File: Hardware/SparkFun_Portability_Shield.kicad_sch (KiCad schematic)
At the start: 39 parts, among them J1 microSD_Friction, SW2 Nav Switch, U4 PCA9557PW, U5 OLED_1.3"

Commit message: Fix nav switch. Adjust silk. Update to v10.
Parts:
- SW2: footprint SparkFun-Switch:Navigation_SMD_9.9x9.9mm -> SparkFun-Switch:Navigation_SMD_7.5x7.5mm; symbol SparkFun-Switch:Navigation_5Way_SMD_9.9x9.9mm -> SparkFun-Switch:Navigation_5Way_SMD_7.5x7.5mm; PROD_ID SWCH-12265 -> SWCH-09905
- U4: value PCA9557PW -> PCA9554PW; symbol SparkFun-IC-Special-Function:PCA9557PW -> SparkFun-IC-Special-Function:PCA9554PW; PROD_ID IC-23355 -> IC-23589
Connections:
- net GND: now also SW2.2 (GND), U4.1 (A0), U4.2 (A1); no longer SW2.10 (GND), SW2.3 (GND), SW2.6 (GND), SW2.8 (GND), SW2.9 (GND), U4.4 (A1), U4.5 (A2)
- net SCL: now also U4.14 (SCL); no longer U4.1 (SCL)
- net SDA: now also U4.15 (SDA); no longer U4.2 (SDA)
- net SD_CD: now also U4.10 (IO5)
- net SW_Center: now also SW2.5 (Center), U4.9 (IO4); no longer SW2.4 (Center), U4.11 (IO4)
- net SW_Down: now also SW2.3 (Down), U4.5 (IO1); no longer SW2.5 (Down), U4.7 (IO1)
- net SW_Left: now also SW2.1 (Left), U4.7 (IO3); no longer SW2.7 (Left), U4.10 (IO3)
- net SW_Right: now also SW2.4 (Right), U4.6 (IO2); no longer SW2.2 (Right), U4.9 (IO2)
- net SW_Up: now also SW2.6 (Up), U4.4 (IO0); no longer SW2.1 (Up), U4.6 (IO0)
- net GPIO_~{INT}: now reaches U4.13 (~{INT})
- net ~{RESET}_P renamed OLED_~{RESET}
- net OLED_~{RESET}: no longer U4.15 (~{RESET})
- no-connect marks 5 -> 4
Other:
- note added: "5-Way Navigation Switch"
- note removed: "D-Pad"
- title: RTK Postcard Portable Shield -> SparkFun Portable Shield
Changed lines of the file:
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@@
 	(paper "USLetter")
 	(title_block
-		(title "RTK Postcard Portable Shield")
+		(title "SparkFun Portable Shield")
 		(date "2024-09-19")
 		(rev "v10")
@@
 	)
 	(no_connect
-		(at 132.08 54.61)
-	)
-	(no_connect
 		(at 132.08 59.69)
 	)
@@
 	(wire
 		(pts
+			(xy 133.35 54.61) (xy 132.08 54.61)
+		)
+		(stroke
+			(width 0)
+			(type default)
+		)
+	)
+	(wire
+		(pts
 			(xy 223.52 46.99) (xy 222.25 46.99)
 		)
@@
 		)
 	)
-	(text "D-Pad"
+	(text "5-Way\nNavigation Switch"
 		(exclude_from_sim no)
 		(at 44.45 20.32 0)
@@
 		)
 	)
+	(global_label "SD_CD"
+		(shape input)
+		(at 133.35 54.61 0)
+		(fields_autoplaced yes)
+		(effects
+			(font
+				(size 1.27 1.27)
+			)
+			(justify left)
+		)
+		(property "Intersheetrefs" "${INTERSHEET_REFS}"
+			(at 142.3223 54.61 0)
+			(effects
+				(font
+					(size 1.27 1.27)
+				)
+				(justify left)
+				(hide yes)
+			)
+		)
+	)
 	(global_label "SCL"
 		(shape input)
@@
 		)
 	)
-	(global_label "~{RESET}_P"
+	(global_label "GPIO_~{INT}"
 		(shape input)
 		(at 110.49 46.99 180)
@@
 		)
 		(property "Intersheetrefs" "${INTERSHEET_REFS}"
-			(at 99.5221 46.99 0)
+			(at 99.159 46.99 0)
 			(effects
 				(font
@@
 		)
 	)
-	(global_label "~{RESET}_P"
+	(global_label "OLED_~{RESET}"
 		(shape input)
 		(at 71.12 118.11 180)
@@
 		)
 		(property "Intersheetrefs" "${INTERSHEET_REFS}"
-			(at 60.1521 118.11 0)
+			(at 56.6445 118.11 0)
 			(effects
 				(font
@@
 	)
 	(symbol
-		(lib_id "SparkFun-Switch:Navigation_5Way_SMD_9.9x9.9mm")
+		(lib_id "SparkFun-Switch:Navigation_5Way_SMD_7.5x7.5mm")
 		(at 44.45 46.99 0)
 		(unit 1)
@@
 		(fields_autoplaced yes)
 		(property "Reference" "SW2"
-			(at 46.1011 58.42 0)
+			(at 46.1011 33.02 0)
 			(effects
 				(font
@@
 		)
 		(property "Value" "Nav Switch"
-			(at 46.1011 60.96 0)
+			(at 46.1011 35.56 0)
 			(effects
 				(font
@@
 			)
 		)
-		(property "Footprint" "SparkFun-Switch:Navigation_SMD_9.9x9.9mm"
+		(property "Footprint" "SparkFun-Switch:Navigation_SMD_7.5x7.5mm"
 			(at 44.45 62.23 0)
 			(effects
@@
 			)
 		)
-		(property "Datasheet" "https://cdn.sparkfun.com/datasheets/Components/Switches/N301102.pdf"
+		(property "Datasheet" "https://cdn.sparkfun.com/assets/c/f/a/b/d/Korean-Hroparts-Elec-K1-5202UA-01.pdf"
 			(at 44.45 67.31 0)
 			(effects
@@
 			)
 		)
-		(property "PROD_ID" "SWCH-12265"
+		(property "PROD_ID" "SWCH-09905"
 			(at 44.45 64.77 0)
 			(effects
@@
 			)
 		)
-		(pin "9"
+		(pin "MP1"
 		)
 		(pin "1"
@@
 		(pin "6"
 		)
-		(pin "7"
-		)
-		(pin "10"
-		)
-		(pin "8"
-		)
 		(pin "3"
 		)
 		(pin "2"
 		)
+		(pin "MP2"
+		)
 		(instances
 			(project ""
@@
 	)
 	(symbol
-		(lib_id "SparkFun-IC-Special-Function:PCA9557PW")
+		(lib_id "SparkFun-IC-Special-Function:PCA9554PW")
 		(at 121.92 49.53 0)
 		(unit 1)
@@
 			)
 		)
-		(property "Value" "PCA9557PW"
+		(property "Value" "PCA9554PW"
 			(at 124.1141 67.31 0)
 			(effects
@@
 			)
 		)
-		(property "Datasheet" "https://www.nxp.com/docs/en/data-sheet/PCA9557.pdf"
+		(property "Datasheet" "https://www.ti.com/lit/ds/symlink/tca9554.pdf"
 			(at 121.92 70.485 0)
 			(effects
@@
 			)
 		)
-		(property "Description" "8-bit I2C-bus and SMBus I/O port with reset, TSSOP-16"
+		(property "Description" "8-bit I2C-bus and SMBus I/O port with interrupt, TSSOP-16"
 			(at 121.92 67.945 0)
 			(effects
@@
 			)
 		)
-		(property "PROD_ID" "IC-23355"
+		(property "PROD_ID" "IC-23589"
 			(at 121.92 73.025 0)
 			(effects
@@
 		)
 		(instances
-			(project "SparkFun_RTK_Postcard_Portable_Shield"
+			(project "SparkFun_Portability_Shield"
 				(path "/e3dd3ae4-244d-4cba-9cca-5d2abf83f29a"
 					(page "2")

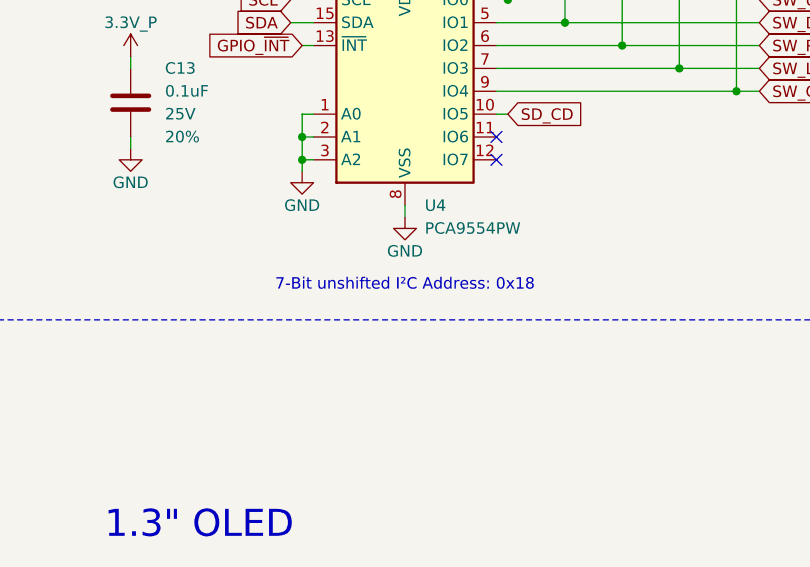
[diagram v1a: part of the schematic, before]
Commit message: Update I2C address on PCA9554
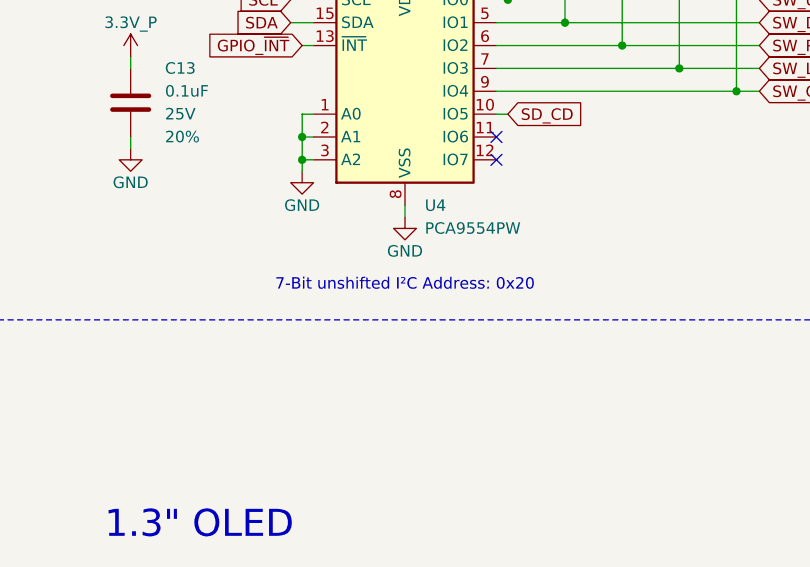
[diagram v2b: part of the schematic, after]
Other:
- note added: "7-Bit unshifted I²C Address: 0x20"
- note removed: "7-Bit unshifted I²C Address: 0x18"
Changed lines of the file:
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@@
 		)
 	)
-	(text "7-Bit unshifted I²C Address: 0x18"
+	(text "7-Bit unshifted I²C Address: 0x20"
 		(exclude_from_sim no)
 		(at 121.92 73.66 0)
